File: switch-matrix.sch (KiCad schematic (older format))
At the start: 112 parts, among them SW1 `, SW10 2, SW11 W, SW12 S, SW13 Y, SW15 3, SW16 E, SW17 D, SW18 X, SW19 4, SW2 TAB, SW20 R, SW21 F, SW22 C, SW23 5, SW24 T, SW25 G, SW26 V, SW27 6, SW28 Z, SW29 H, SW3 ESC, SW30 B, SW31 Space, SW32 7, SW33 U, SW34 J, SW35 N, SW36 8, SW37 I, SW38 K, SW39 M, SW40 9, SW41 O, SW42 L, SW43 ,, SW44 0, SW45 P, SW46 ;, SW47 ., SW49 -, SW50 [, SW51 ', SW52 /, SW54 =, SW55 ], SW56 \\, SW58 Backspace, SW59 Enter, SW6 1, SW7 Q, SW8 A, U2 74LS138, U3 74LS138

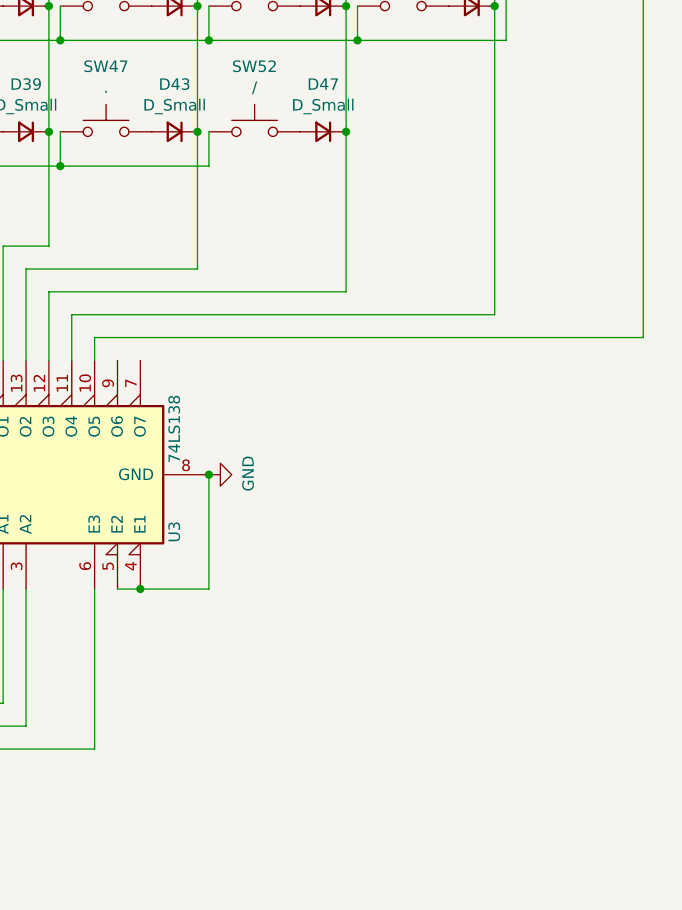
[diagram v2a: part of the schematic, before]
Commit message: Rotary Encoder added
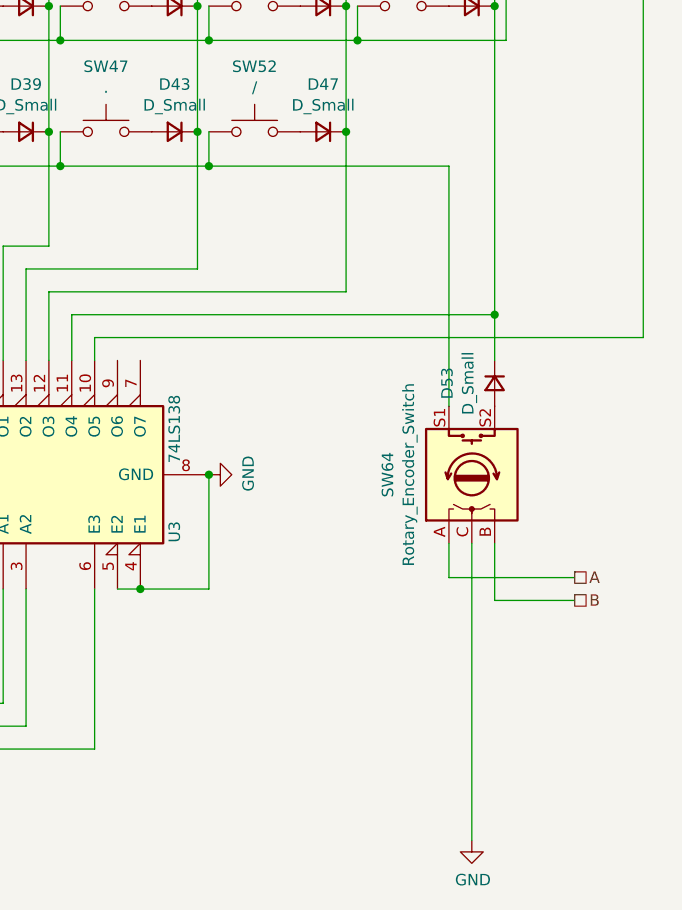
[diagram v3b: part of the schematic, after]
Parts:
- added D53: D_Small, Diode_SMD:D_SOD-323_HandSoldering, symbol Device:D_Small
- added SW64: Rotary_Encoder_Switch, Rotary_Encoder:RotaryEncoder_Alps_EC11E-Switch_Vertical_H20mm_CircularMountingHoles, symbol Device:Rotary_Encoder_Switch
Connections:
- net GND: now also SW64.C
- net at R4.1, SW13.1, SW18.1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: now also SW64.S1
- net at D48.1 (K), D49.1 (K), D50.1 (K)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: now also D53.1 (K)
- new net: D53.2 (A), SW64.S2
- new net A: SW64.A
- new net B: SW64.B
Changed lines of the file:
@@
 Wire Wire Line
 	9600 1200 9600 1750
+$Comp
+L Device:Rotary_Encoder_Switch SW64
+U 1 1 60D74750
+P 10150 4350
+F 0 "SW64" H 10150 4717 50  0000 C CNN
+F 1 "Rotary_Encoder_Switch" H 10150 4626 50  0000 C CNN
+F 2 "Rotary_Encoder:RotaryEncoder_Alps_EC11E-Switch_Vertical_H20mm_CircularMountingHoles" H 10000 4510 50  0001 C CNN
+F 3 "~" H 10150 4610 50  0001 C CNN
+	1    10150 4350
+	0    -1   -1   0
+$EndComp
+$Comp
+L Device:D_Small D53
+U 1 1 60DBA6A2
+P 10250 3950
+F 0 "D53" H 10250 3743 50  0000 C CNN
+F 1 "D_Small" H 10250 3834 50  0000 C CNN
+F 2 "Diode_SMD:D_SOD-323_HandSoldering" V 10250 3950 50  0001 C CNN
+F 3 "~" V 10250 3950 50  0001 C CNN
+	1    10250 3950
+	0    1    1    0
+$EndComp
+Wire Wire Line
+	10250 3650 10250 3850
+Connection ~ 10250 3650
+Wire Wire Line
+	10050 4050 10050 3000
+Wire Wire Line
+	10050 3000 9000 3000
+Connection ~ 9000 3000
+Text HLabel 10600 4800 2    50   UnSpc ~ 0
+A
+Text HLabel 10600 4900 2    50   UnSpc ~ 0
+B
+Wire Wire Line
+	10600 4800 10050 4800
+Wire Wire Line
+	10050 4800 10050 4650
+Wire Wire Line
+	10250 4650 10250 4900
+Wire Wire Line
+	10250 4900 10600 4900
+Wire Wire Line
+	10150 4650 10150 5950
+$Comp
+L power:GND #PWR0131
+U 1 1 60F3603C
+P 10150 5950
+F 0 "#PWR0131" H 10150 5700 50  0001 C CNN
+F 1 "GND" H 10155 5777 50  0000 C CNN
+F 2 "" H 10150 5950 50  0001 C CNN
+F 3 "" H 10150 5950 50  0001 C CNN
+	1    10150 5950
+	1    0    0    -1
+$EndComp
 $EndSCHEMATC

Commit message: Routing angefangen
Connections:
- net at R2.1, SW11.1, SW16.1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: now also SW64.S1
- net at R4.1, SW13.1, SW18.1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: no longer SW64.S1
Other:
- moved on the sheet: D52, SW59
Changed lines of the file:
@@
 L Switch:SW_Push SW59
 U 1 1 60799DB7
-P 10500 2000
-F 0 "SW59" H 10500 2285 50  0000 C CNN
-F 1 "Enter" H 10500 2194 50  0000 C CNN
-F 2 "msp430_Keyboard:Kailh_MX_Socket" H 10500 2200 50  0001 C CNN
-F 3 "~" H 10500 2200 50  0001 C CNN
-	1    10500 2000
+P 10500 2700
+F 0 "SW59" H 10500 2985 50  0000 C CNN
+F 1 "Enter" H 10500 2894 50  0000 C CNN
+F 2 "msp430_Keyboard:Kailh_MX_Socket" H 10500 2900 50  0001 C CNN
+F 3 "~" H 10500 2900 50  0001 C CNN
+	1    10500 2700
 	1    0    0    -1
 $EndComp
@@
 	9650 1900 9000 1900
 Wire Wire Line
-	10300 2000 10300 2450
-Wire Wire Line
-	10300 2450 9650 2450
-Wire Wire Line
 	1850 2300 1850 2450
 Connection ~ 1850 2450
@@
 Wire Wire Line
 	9650 2300 9650 2450
-Connection ~ 9650 2450
 Wire Wire Line
 	9650 2450 9000 2450
@@
 L Device:D_Small D52
 U 1 1 60F82724
-P 10800 2000
-F 0 "D52" H 10800 1793 50  0000 C CNN
-F 1 "D_Small" H 10800 1884 50  0000 C CNN
-F 2 "Diode_SMD:D_SOD-323_HandSoldering" V 10800 2000 50  0001 C CNN
-F 3 "~" V 10800 2000 50  0001 C CNN
-	1    10800 2000
+P 10800 2700
+F 0 "D52" H 10800 2493 50  0000 C CNN
+F 1 "D_Small" H 10800 2584 50  0000 C CNN
+F 2 "Diode_SMD:D_SOD-323_HandSoldering" V 10800 2700 50  0001 C CNN
+F 3 "~" V 10800 2700 50  0001 C CNN
+	1    10800 2700
 	-1   0    0    1
 $EndComp
@@
 Wire Wire Line
 	10250 1750 10250 2300
-Connection ~ 10250 2300
-Wire Wire Line
-	10250 2300 10250 3650
-Wire Wire Line
-	10900 1200 10900 2000
+Wire Wire Line
+	10900 1200 10900 2700
 Wire Wire Line
 	10900 3750 8500 3750
 Wire Wire Line
 	8500 3750 8500 3850
-Connection ~ 10900 2000
-Wire Wire Line
-	10900 2000 10900 3750
+Connection ~ 10900 2700
+Wire Wire Line
+	10900 2700 10900 3750
 Wire Wire Line
 	7700 4350 7700 5700
@@
 Wire Wire Line
 	10250 3650 10250 3850
-Connection ~ 10250 3650
-Wire Wire Line
-	10050 4050 10050 3000
-Wire Wire Line
-	10050 3000 9000 3000
-Connection ~ 9000 3000
 Text HLabel 10600 4800 2    50   UnSpc ~ 0
 A
@@
 	1    0    0    -1
 $EndComp
+Wire Wire Line
+	10050 2450 10350 2450
+Wire Wire Line
+	10350 2450 10350 1900
+Wire Wire Line
+	10350 1900 9650 1900
+Wire Wire Line
+	10050 2450 10050 4050
+Connection ~ 9650 1900
+Connection ~ 10250 3650
+Connection ~ 10250 2300
+Wire Wire Line
+	10250 2300 10250 3650
+Wire Wire Line
+	10300 2700 9850 2700
+Wire Wire Line
+	9850 2700 9850 2450
+Wire Wire Line
+	9850 2450 9650 2450
+Connection ~ 9650 2450
 $EndSCHEMATC

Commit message: Layout sent to JLCPCB
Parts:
- C1, C2: footprint Capacitor_SMD:C_0603_1608Metric -> Capacitor_SMD:C_0603_1608Metric_Pad1.08x0.95mm_HandSolder
- R1, R2, R3, R4: footprint Resistor_SMD:R_0603_1608Metric -> Resistor_SMD:R_0603_1608Metric_Pad0.98x0.95mm_HandSolder
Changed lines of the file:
@@
 F 0 "C1" V 3250 5650 50  0000 L CNN
 F 1 "100n" V 3250 5850 50  0000 L CNN
-F 2 "Capacitor_SMD:C_0603_1608Metric" H 3300 5800 50  0001 C CNN
+F 2 "Capacitor_SMD:C_0603_1608Metric_Pad1.08x0.95mm_HandSolder" H 3300 5800 50  0001 C CNN
 F 3 "~" H 3300 5800 50  0001 C CNN
 	1    3300 5800
@@
 F 0 "C2" V 7650 5650 50  0000 L CNN
 F 1 "100n" V 7650 5850 50  0000 L CNN
-F 2 "Capacitor_SMD:C_0603_1608Metric" H 7700 5800 50  0001 C CNN
+F 2 "Capacitor_SMD:C_0603_1608Metric_Pad1.08x0.95mm_HandSolder" H 7700 5800 50  0001 C CNN
 F 3 "~" H 7700 5800 50  0001 C CNN
 	1    7700 5800
@@
 F 0 "R1" V 1454 1350 50  0000 C CNN
 F 1 "22" V 1545 1350 50  0000 C CNN
-F 2 "Resistor_SMD:R_0603_1608Metric" H 1650 1350 50  0001 C CNN
+F 2 "Resistor_SMD:R_0603_1608Metric_Pad0.98x0.95mm_HandSolder" H 1650 1350 50  0001 C CNN
 F 3 "~" H 1650 1350 50  0001 C CNN
 	1    1650 1350
@@
 F 0 "R2" V 1454 1900 50  0000 C CNN
 F 1 "22" V 1545 1900 50  0000 C CNN
-F 2 "Resistor_SMD:R_0603_1608Metric" H 1650 1900 50  0001 C CNN
+F 2 "Resistor_SMD:R_0603_1608Metric_Pad0.98x0.95mm_HandSolder" H 1650 1900 50  0001 C CNN
 F 3 "~" H 1650 1900 50  0001 C CNN
 	1    1650 1900
@@
 F 0 "R3" V 1454 2450 50  0000 C CNN
 F 1 "22" V 1545 2450 50  0000 C CNN
-F 2 "Resistor_SMD:R_0603_1608Metric" H 1650 2450 50  0001 C CNN
+F 2 "Resistor_SMD:R_0603_1608Metric_Pad0.98x0.95mm_HandSolder" H 1650 2450 50  0001 C CNN
 F 3 "~" H 1650 2450 50  0001 C CNN
 	1    1650 2450
@@
 F 0 "R4" V 1454 3000 50  0000 C CNN
 F 1 "22" V 1545 3000 50  0000 C CNN
-F 2 "Resistor_SMD:R_0603_1608Metric" H 1650 3000 50  0001 C CNN
+F 2 "Resistor_SMD:R_0603_1608Metric_Pad0.98x0.95mm_HandSolder" H 1650 3000 50  0001 C CNN
 F 3 "~" H 1650 3000 50  0001 C CNN
 	1    1650 3000

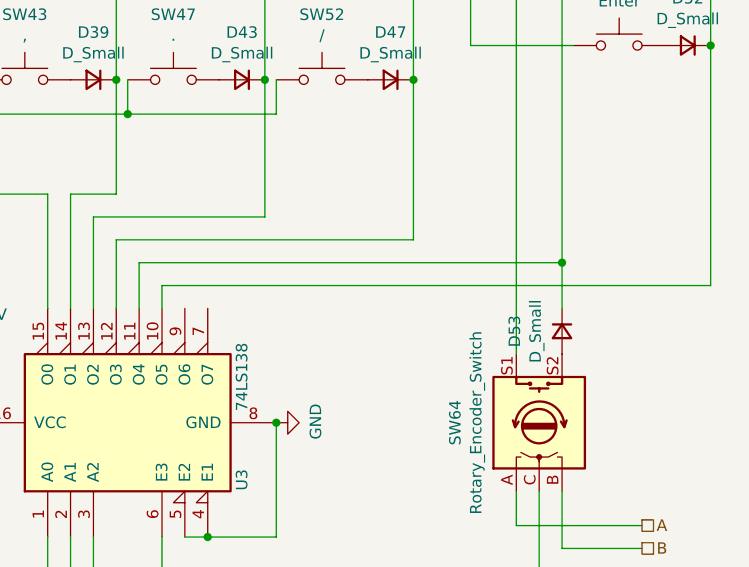
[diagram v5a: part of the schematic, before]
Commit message: Filterung in den USB-Leitungen, VBus besser abgeblockt, Enter Taste gedreht
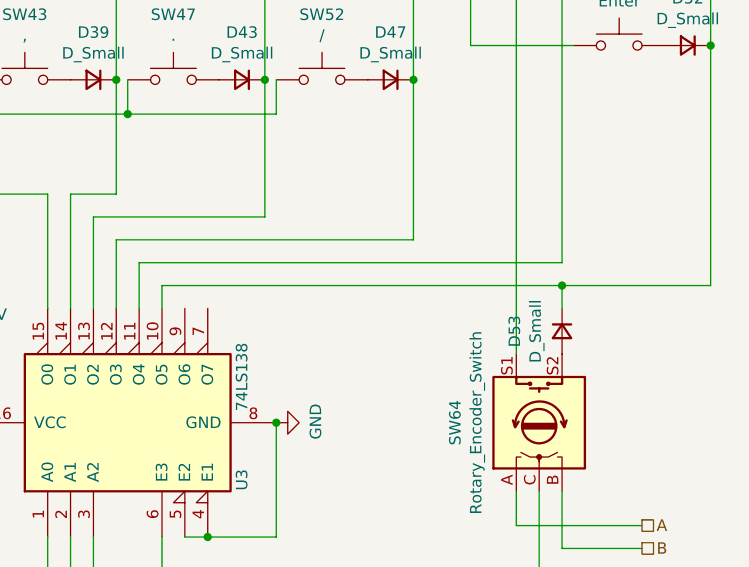
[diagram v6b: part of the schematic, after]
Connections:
- net at D51.1 (K), D52.1 (K), U3.10 (O5): now also D53.1 (K)
- net at D48.1 (K), D49.1 (K), D50.1 (K)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: no longer D53.1 (K)
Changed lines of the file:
@@
 	10900 1200 10900 2700
 Wire Wire Line
-	10900 3750 8500 3750
+	10900 3750 10250 3750
 Wire Wire Line
 	8500 3750 8500 3850
@@
 	0    1    1    0
 $EndComp
-Wire Wire Line
-	10250 3650 10250 3850
 Text HLabel 10600 4800 2    50   UnSpc ~ 0
 A
@@
 	10050 2450 10050 4050
 Connection ~ 9650 1900
-Connection ~ 10250 3650
 Connection ~ 10250 2300
 Wire Wire Line
@@
 	9850 2450 9650 2450
 Connection ~ 9650 2450
+Wire Wire Line
+	10250 3850 10250 3750
+Connection ~ 10250 3750
+Wire Wire Line
+	10250 3750 8500 3750
 $EndSCHEMATC
